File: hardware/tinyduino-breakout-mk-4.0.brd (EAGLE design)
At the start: 20 x 20 mm, 3 parts

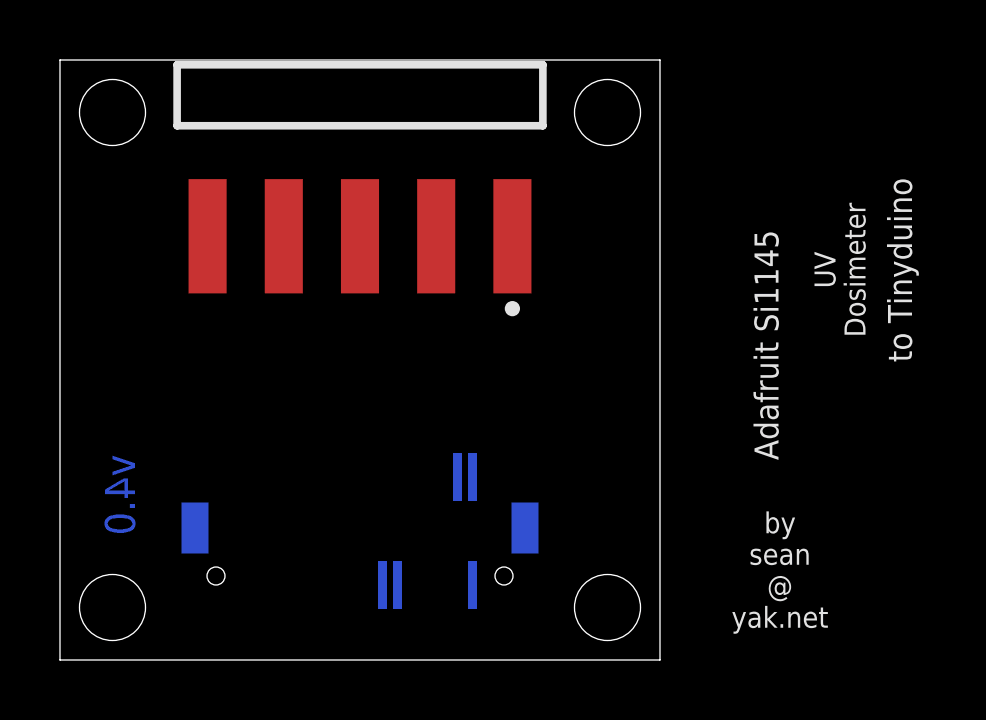
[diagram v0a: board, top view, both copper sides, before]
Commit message: finished layout but unhappy w/choices
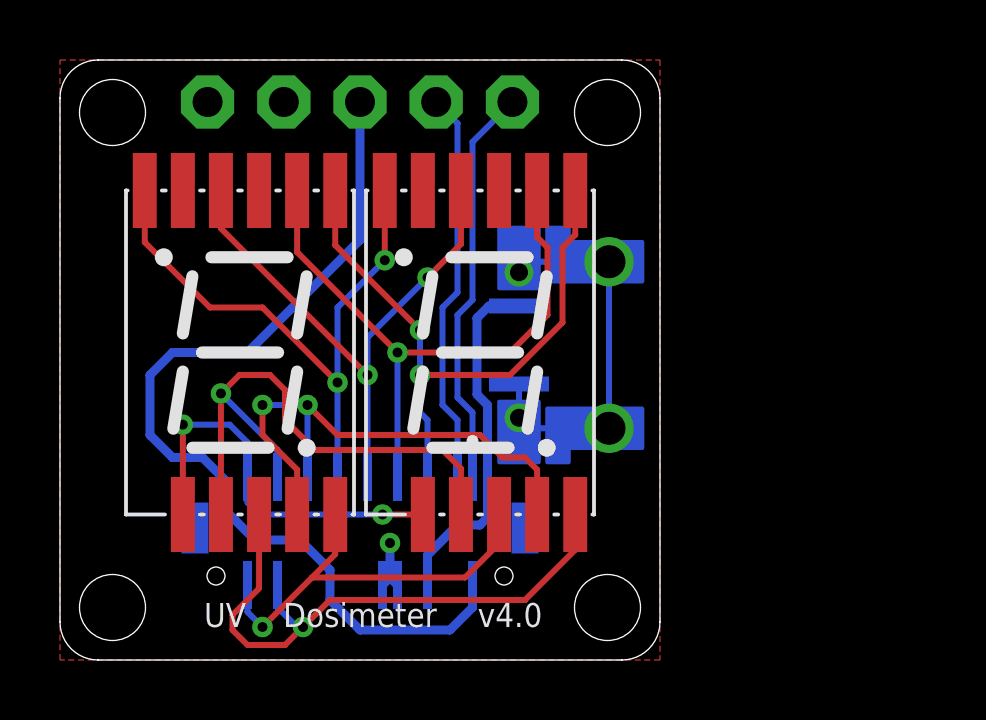
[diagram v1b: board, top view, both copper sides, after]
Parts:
- removed I2C1: M04-I2CTINYDUINO-CONNECTOR-REV, A_butts:DF12-32-DP-I2CONLY-REV
- added DIGIT1, DIGIT2: 7SEG_1DIG_2DP7MM_CC_SMT, a_parts:7SEG_1DIG_7MM_SMT
- added J1: DF12-32-DP-NOTREALLYREV, a_parts:DF12-32-DP-I2C+EXTRA-REV
- added USB1: USB_AB_PWRONLY, a_parts:FCI-10103594-USB-MICRO-B-PWRONLY
- JP1: value M05SMD-SHORT -> M05PTH-CENTERED; device A_butts:1X05-SMD-SHORT -> a_parts:1X05_PTH_CENTERED
- moved JP1 1.30 mm to (10.0, 18.6), flipped to the bottom, turned to 0 degrees
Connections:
- new net 5V: J1.8, USB1.1
- new net AD0: DIGIT1.5, DIGIT2.5, J1.11
- new net AD2: DIGIT1.6, DIGIT2.6, J1.7
- new net IO2: DIGIT1.9, DIGIT2.7, J1.28
- new net IO4: DIGIT1.7, DIGIT2.9, J1.32
- new net IO5: DIGIT1.11, DIGIT2.11, J1.31
- new net IO7: DIGIT1.10, DIGIT2.10, J1.27
- new net IO9: DIGIT1.8, DIGIT2.8, J1.23
- new net MOSI: DIGIT1.1, DIGIT2.1, J1.19
- new net SCK: DIGIT1.3, DIGIT2.3, J1.15
- net GND: now also J1.12, J1.14, USB1.5, USB1.SHIELD@1, USB1.SHIELD@2, USB1.SHIELD@3, USB1.SHIELD@4; no longer I2C1.12, I2C1.14
- net SCL: now also J1.1; no longer I2C1.1
- net SDA: now also J1.3; no longer I2C1.3
- net VCC: now also J1.2; no longer I2C1.2
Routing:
- net VCC: track 0.00 -> 31.1 mm
- net AD2: track 0.00 -> 20.9 mm, vias 0 -> 2
- net AD0: track 0.00 -> 20.7 mm, vias 0 -> 1
- net MOSI: track 0.00 -> 20.3 mm, vias 0 -> 2
- net IO2: track 0.00 -> 20.2 mm, vias 0 -> 1
- net IO7: track 0.00 -> 19.3 mm, vias 0 -> 1
- net SCK: track 0.00 -> 19.0 mm, vias 0 -> 2
- net IO9: track 0.00 -> 18.1 mm, vias 0 -> 2
- net GND: track 0.00 -> 14.8 mm, vias 0 -> 1
- net IO4: track 0.00 -> 14.0 mm, vias 0 -> 1
- net SCL: track 0.00 -> 13.5 mm
- net IO5: track 0.00 -> 13.4 mm, vias 0 -> 2
- net SDA: track 0.00 -> 13.2 mm
- net 5V: track 0.00 -> 11.9 mm
- added copper zone on layer 1, net GND
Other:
- outline, holes or cut-outs redrawn
